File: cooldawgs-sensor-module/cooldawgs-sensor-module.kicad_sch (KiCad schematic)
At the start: 5 parts, among them U1 XIAO-nRF52840-DIP, U2 MLX90614ESF-AAA-000-TU, U3 DHT22

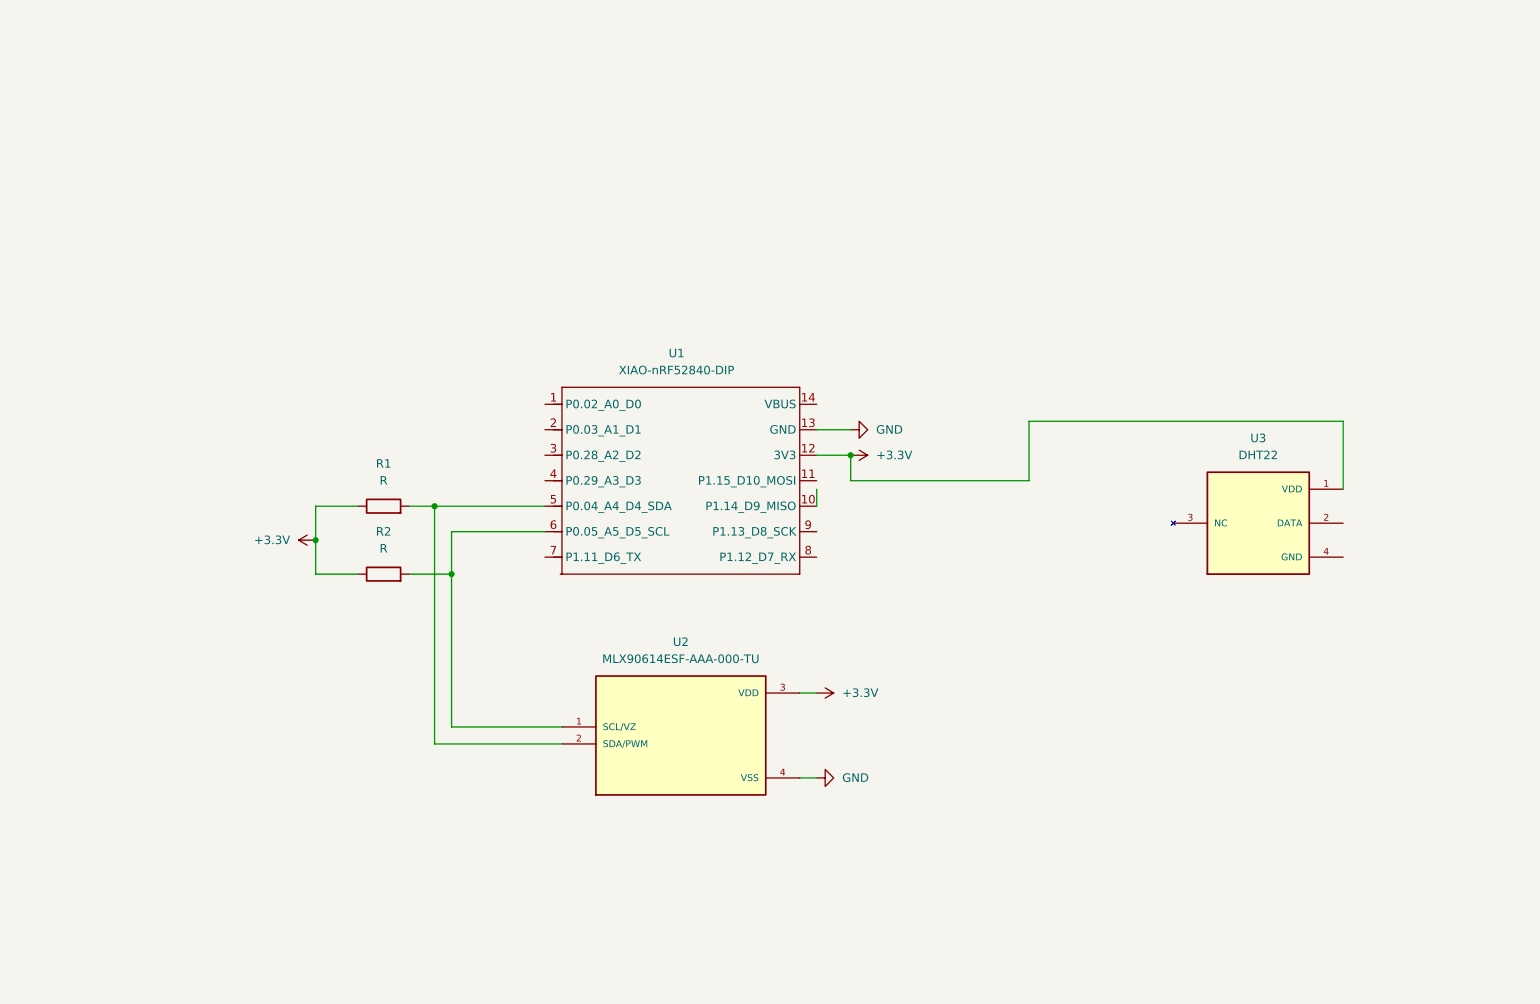
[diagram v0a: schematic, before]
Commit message: added all sensors and created initial pcb
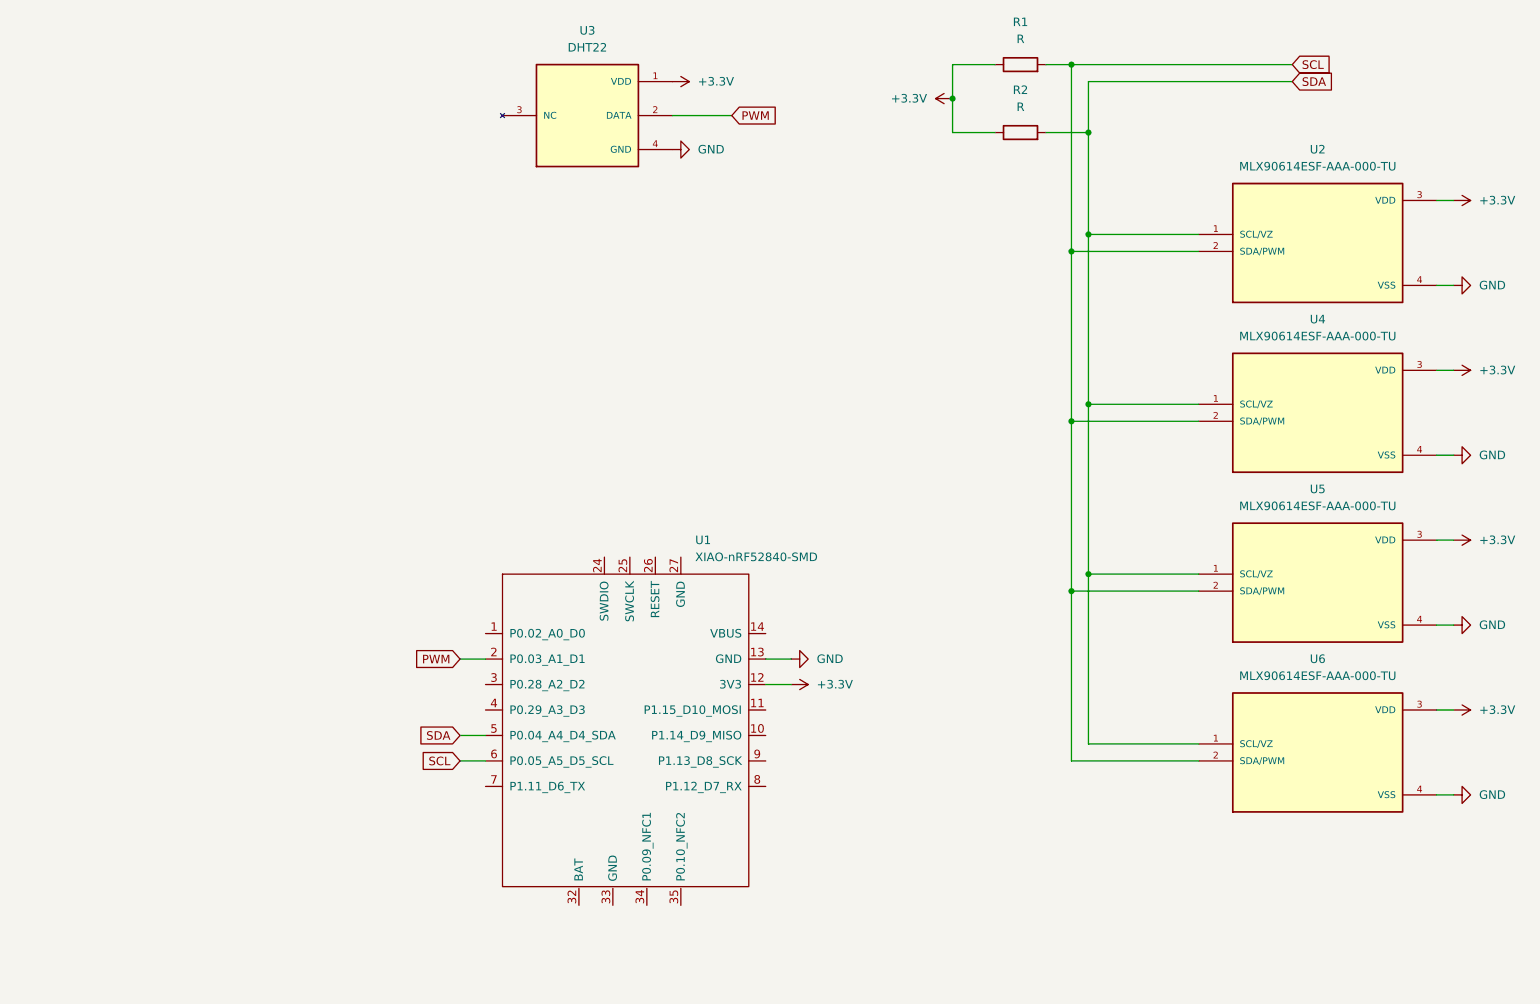
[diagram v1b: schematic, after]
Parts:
- removed U1: XIAO-nRF52840-DIP, XIAO_Series_Footprints:XIAO-nRF52840-DIP, symbol Seeed_Studio_XIAO_Series:XIAO-nRF52840-DIP
- added U1: XIAO-nRF52840-SMD, XIAO_Series_Footprints:XIAO-nRF52840-SMD, symbol Seeed_Studio_XIAO_Series:XIAO-nRF52840-SMD
- added U4, U5, U6: MLX90614ESF-AAA-000-TU, MLX90614ESF-AAA-000-TU:TO254P912H435-4, symbol MLX90614ESF-AAA-000-TU:MLX90614ESF-AAA-000-TU
- R1, R2: footprint Resistor_THT:R_Axial_DIN0207_L6.3mm_D2.5mm_P2.54mm_Vertical -> Resistor_THT:R_Axial_DIN0207_L6.3mm_D2.5mm_P7.62mm_Horizontal
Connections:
- net +3.3V: now also U1.12 (3V3), U4.3 (VDD), U5.3 (VDD), U6.3 (VDD)
- net GND: now also U3.4 (GND), U1.13 (GND), U4.4 (VSS), U5.4 (VSS), U6.4 (VSS)
- net SDA: now reaches R2.2, U2.1 (SCL/VZ)
- net SDA: now also U1.5 (P0.04_A4_D4_SDA), U4.1 (SCL/VZ), U5.1 (SCL/VZ), U6.1 (SCL/VZ)
- net SCL: now reaches R1.2, U2.2 (SDA/PWM)
- net SCL: now also U1.6 (P0.05_A5_D5_SCL), U4.2 (SDA/PWM), U5.2 (SDA/PWM), U6.2 (SDA/PWM)
- net PWM: now reaches U3.2 (DATA)
- net PWM: now also U1.2 (P0.03_A1_D1)
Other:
- moved on the sheet: R1, R2, U2, U3

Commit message: added step 3d file of current pcb
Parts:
- added R3: R, Resistor_THT:R_Axial_DIN0207_L6.3mm_D2.5mm_P7.62mm_Horizontal, symbol Device:R
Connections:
- net +3.3V: now also R3.2
- net PWM: now also R3.1
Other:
- moved on the sheet: U1

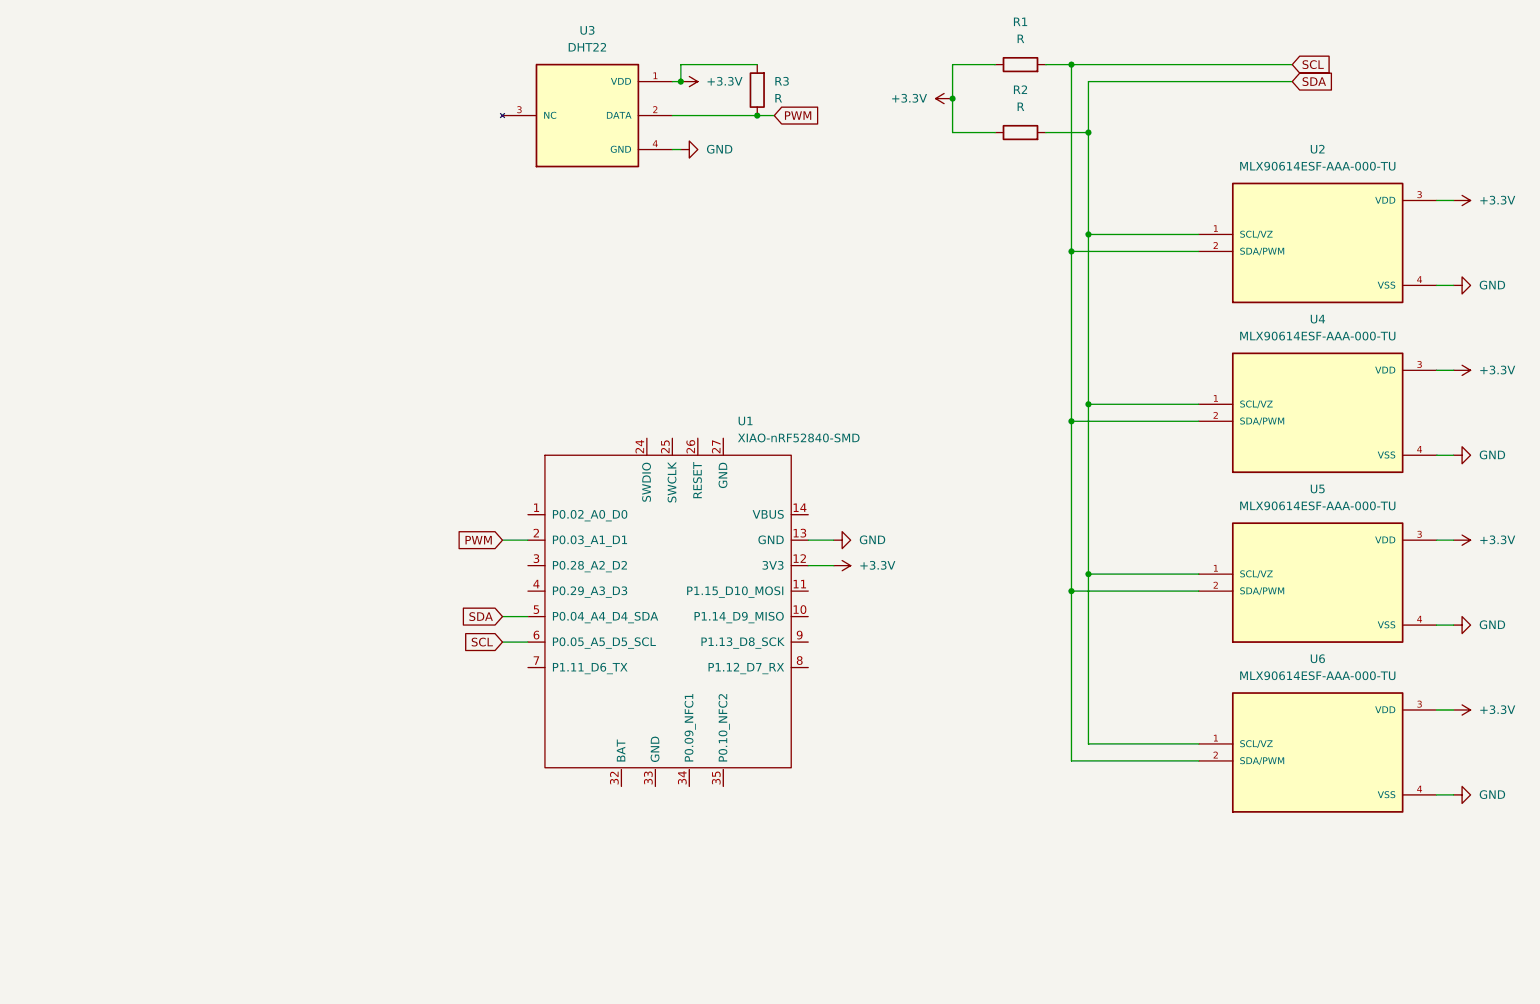
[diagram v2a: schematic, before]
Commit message: added battery from braxton
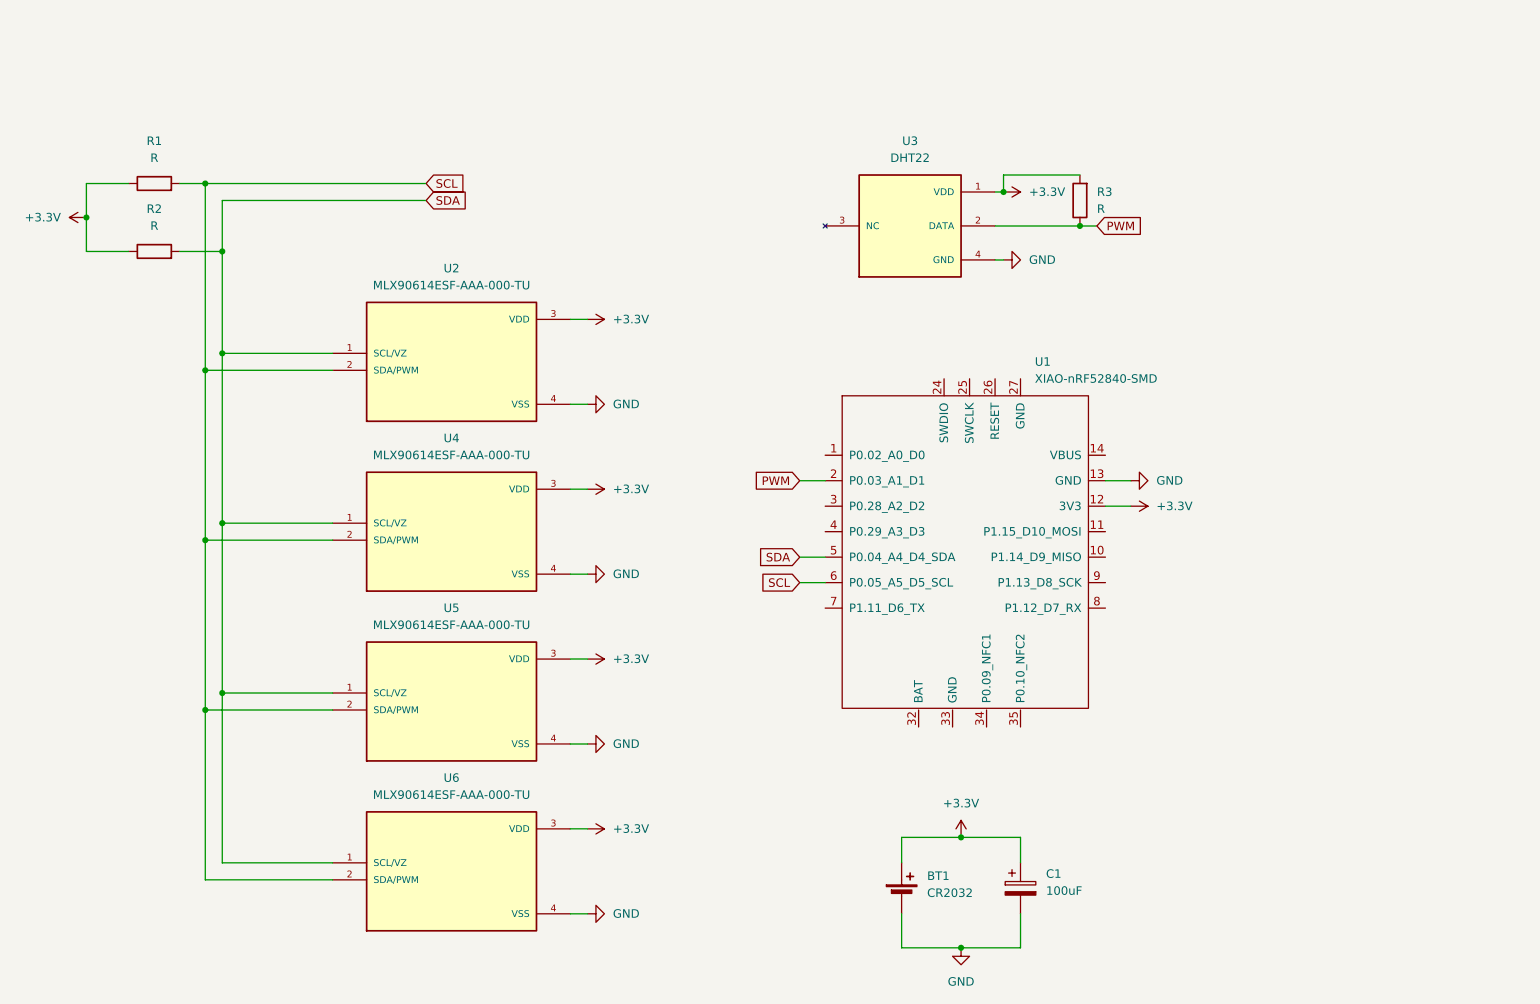
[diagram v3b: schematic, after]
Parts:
- added BT1: CR2032, Battery:BatteryHolder_Keystone_3034_1x20mm, symbol Device:Battery_Cell
- added C1: 100uF, Capacitor_THT:CP_Radial_D5.0mm_P2.00mm, symbol Device:C_Polarized
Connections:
- net +3.3V: now also BT1.1 (+), C1.1
- net GND: now also BT1.2 (-), C1.2
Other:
- moved on the sheet: R1, R2, R3, U1, U2, U3, U4, U5, U6
